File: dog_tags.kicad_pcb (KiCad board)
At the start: 4 copper layers, 0 parts

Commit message: Basic layout for PCB done, including silkscreen
Signed-off-by: Lucy Mielke <user@domain.tld>
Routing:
- added copper zone on F.Cu, net (none)
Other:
- board outline added: 49.4 x 28.1 mm
- board text added: "THIS MACHINE KILLS FASCISTS"
- board text added: "engineering.redlucy404.de"

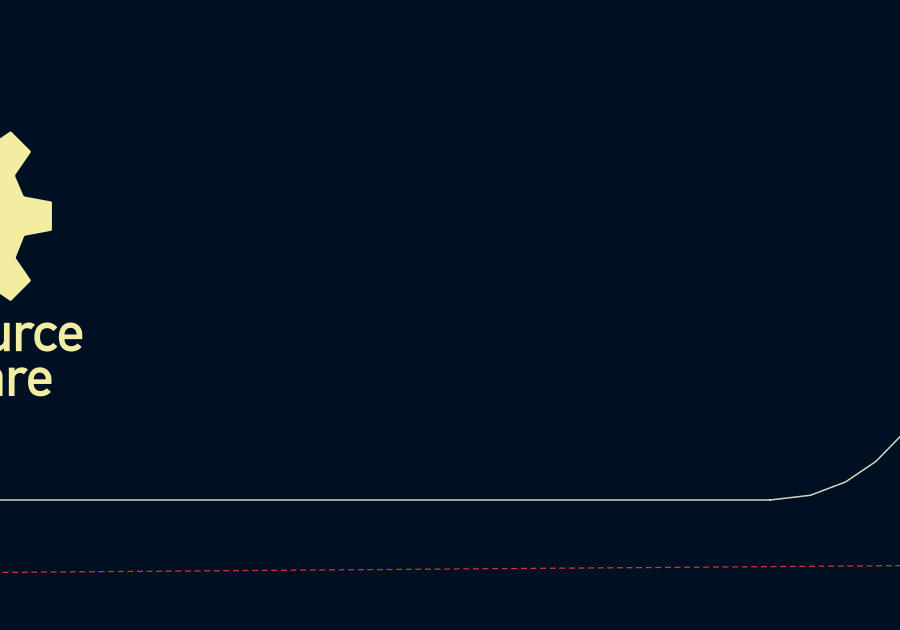
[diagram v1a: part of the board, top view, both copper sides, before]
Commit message: RFID IC placement + keep-out zone
Signed-off-by: Lucy Mielke <user@domain.tld>
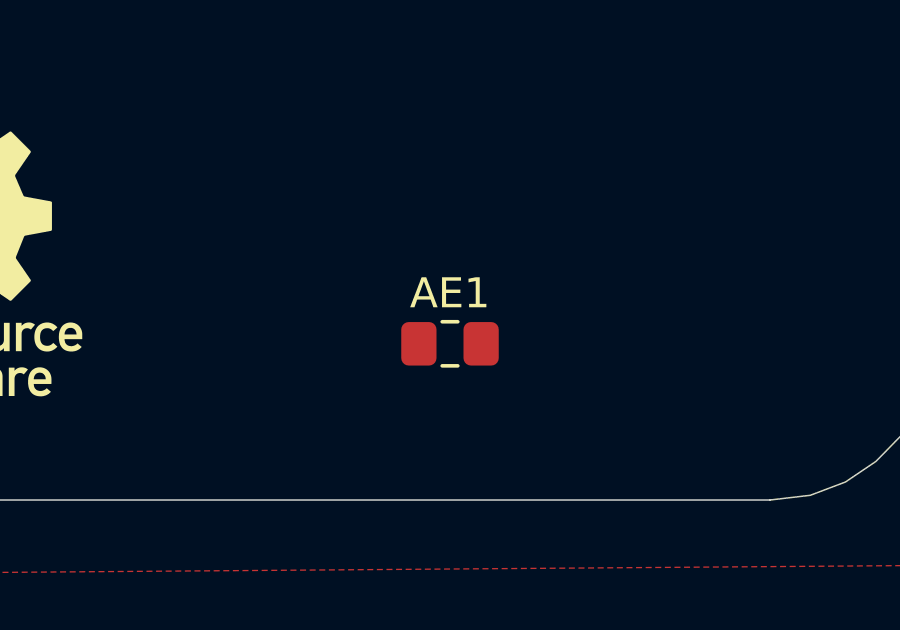
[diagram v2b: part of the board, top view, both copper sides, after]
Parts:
- added AE1: LXMS21ACMD-220, Capacitor_SMD:C_0805_2012Metric_Pad1.18x1.45mm_HandSolder, F.Cu at (145.0, 94.2)
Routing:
- added copper zone on F.Cu, net GND
- removed copper zone on F.Cu, net (none)
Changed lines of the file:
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@@
 		(13 "F.Paste" user)
 		(15 "B.Paste" user)
-		(5 "F.SilkS" user)
-		(7 "B.SilkS" user)
+		(5 "F.SilkS" user "F.Silkscreen")
+		(7 "B.SilkS" user "B.Silkscreen")
 		(1 "F.Mask" user)
 		(3 "B.Mask" user)
 		(25 "Edge.Cuts" user)
 		(27 "Margin" user)
-		(31 "F.CrtYd" user)
-		(29 "B.CrtYd" user)
+		(31 "F.CrtYd" user "F.Courtyard")
+		(29 "B.CrtYd" user "B.Courtyard")
 		(35 "F.Fab" user)
 	)
@@
 		(capping no)
 		(filling no)
-		(zone_defaults)
 		(pcbplotparams
 			(layerselection 0x00000000_00000000_55555555_5755f5ff)
@@
 	(property "REVISION" "1.0")
 	(property "TITLE" "Dog Tags")
+	(footprint "Capacitor_SMD:C_0805_2012Metric_Pad1.18x1.45mm_HandSolder"
+		(layer "F.Cu")
+		(at 145.034 94.234)
+		(descr "Capacitor SMD 0805 (2012 Metric), square (rectangular) end terminal, IPC-7351 nominal with elongated pad for handsoldering. (Body size source: IPC-SM-782 page 76, https://www.pcb-3d.com/wordpress/wp-content/uploads/ipc-sm-782a_amendment_1_and_2.pdf, https://docs.google.com/spreadsheets/d/1BsfQQcO9C6DZCsRaXUlFlo91Tg2WpOkGARC1WS5S8t0/edit?usp=sharing)")
+		(tags "capacitor handsolder")
+		(property "Reference" "AE1"
+			(at 0 -1.68 0)
+			(layer "F.SilkS")
+			(effects
+				(font
+					(size 1 1)
+					(thickness 0.15)
+				)
+			)
+		)
+		(property "Value" "LXMS21ACMD-220"
+			(at 0 1.68 0)
+			(layer "F.Fab")
+			(effects
+				(font
+					(size 1 1)
+					(thickness 0.15)
+				)
+			)
+		)
+		(property "Datasheet" ""
+			(at 0 0 0)
+			(layer "F.Fab")
+			(hide yes)
+			(effects
+				(font
+					(size 1.27 1.27)
+				)
+			)
+		)
+		(property "Description" "Dipole antenna"
+			(at 0 0 0)
+			(layer "F.Fab")
+			(hide yes)
+			(effects
+				(font
+					(size 1.27 1.27)
+				)
+			)
+		)
+		(property "KiLib_Generator" "SMD_2terminal_chip_molded"
+			(at 0 0 0)
+			(layer "F.SilkS")
+			(hide yes)
+			(effects
+				(font
+					(size 1 1)
+					(thickness 0.15)
+				)
+			)
+		)
+		(sheetname "/")
+		(sheetfile "dog_tags.kicad_sch")
+		(units
+			(unit
+				(name "A")
+				(pins "1" "2")
+			)
+		)
+		(attr smd)
+		(duplicate_pad_numbers_are_jumpers no)
+		(fp_line
+			(start -0.261252 -0.735)
+			(end 0.261252 -0.735)
+			(stroke
+				(width 0.12)
+				(type solid)
+			)
+			(layer "F.SilkS")
+		)
+		(fp_line
+			(start -0.261252 0.735)
+			(end 0.261252 0.735)
+			(stroke
+				(width 0.12)
+				(type solid)
+			)
+			(layer "F.SilkS")
+		)
+		(fp_rect
+			(start -1.88 -0.98)
+			(end 1.88 0.98)
+			(stroke
+				(width 0.05)
+				(type solid)
+			)
+			(fill no)
+			(layer "F.CrtYd")
+		)
+		(fp_rect
+			(start -1 -0.625)
+			(end 1 0.625)
+			(stroke
+				(width 0.1)
+				(type solid)
+			)
+			(fill no)
+			(layer "F.Fab")
+		)
+		(fp_text user "${REFERENCE}"
+			(at 0 0 0)
+			(layer "F.Fab")
+			(effects
+				(font
+					(size 0.5 0.5)
+					(thickness 0.08)
+				)
+			)
+		)
+		(pad "1" smd roundrect
+			(at -1.0375 0)
+			(size 1.175 1.45)
+			(layers "F.Cu" "F.Mask" "F.Paste")
+			(roundrect_rratio 0.212766)
+			(net "GND")
+			(pintype "input")
+		)
+		(pad "2" smd roundrect
+			(at 1.0375 0)
+			(size 1.175 1.45)
+			(layers "F.Cu" "F.Mask" "F.Paste")
+			(roundrect_rratio 0.212766)
+			(net "GND")
+			(pintype "input")
+		)
+		(embedded_fonts no)
+		(model "${KICAD10_3DMODEL_DIR}/Capacitor_SMD.3dshapes/C_0805_2012Metric.step"
+			(offset
+				(xyz 0 0 0)
+			)
+			(scale
+				(xyz 1 1 1)
+			)
+			(rotate
+				(xyz 0 0 0)
+			)
+		)
+	)
 	(gr_poly
 		(pts
@@
 	)
 	(zone
+		(net "GND")
 		(layer "F.Cu")
 		(name "copper pour")
@@
 			)
 		)
+	)
+	(zone
+		(layers "F.Cu" "B.Cu" "In1.Cu" "In2.Cu")
+		(name "Antenna Keep-Out Zone")
+		(hatch edge 0.5)
+		(connect_pads
+			(clearance 0)
+		)
+		(min_thickness 0.25)
+		(keepout
+			(tracks allowed)
+			(vias allowed)
+			(pads allowed)
+			(copperpour not_allowed)
+			(footprints allowed)
+		)
+		(placement
+			(enabled no)
+			(sheetname "/")
+		)
+		(fill
+			(thermal_gap 0.5)
+			(thermal_bridge_width 0.5)
+			(island_removal_mode 1)
+		)
+		(polygon
+			(pts
+				(xy 139.907 88.941) (xy 149.907 88.941) (xy 149.907 99.441) (xy 139.907 99.441)
+			)
+		)

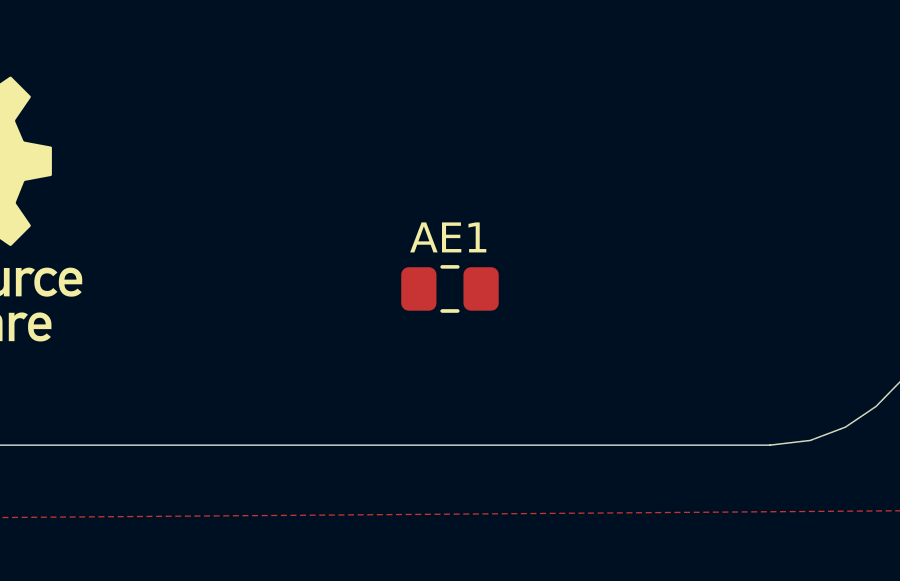
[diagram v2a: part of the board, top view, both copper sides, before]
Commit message: Route antenna trace
Signed-off-by: Lucy Mielke <user@domain.tld>
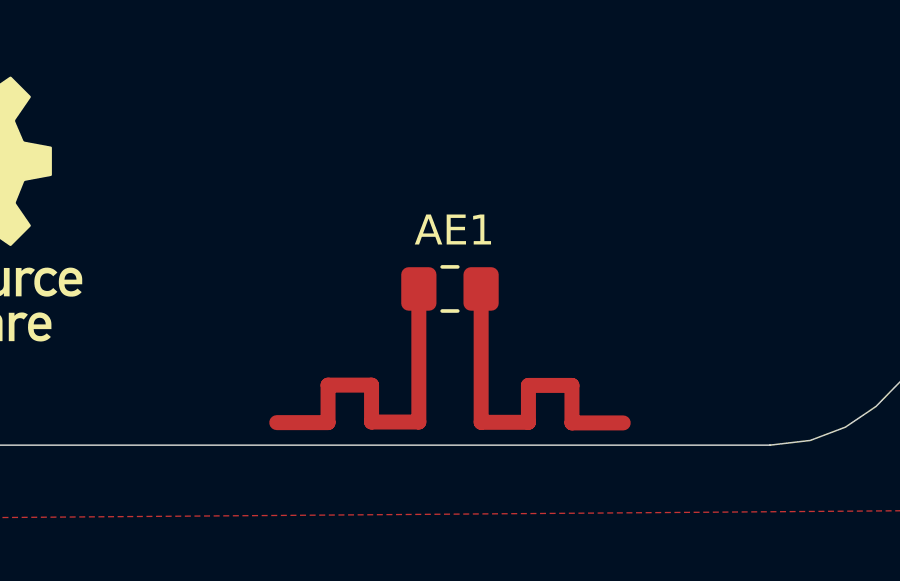
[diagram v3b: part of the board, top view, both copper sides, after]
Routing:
- net GND: track 0.00 -> 23.3 mm

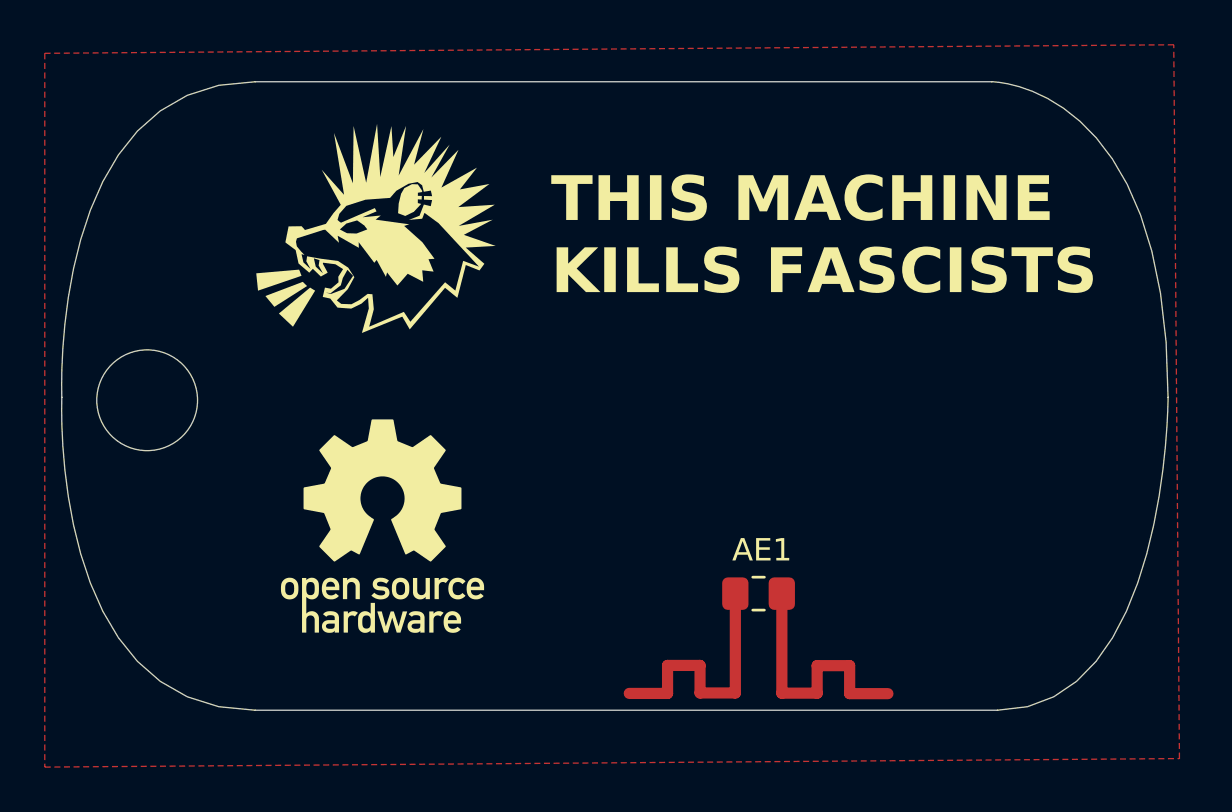
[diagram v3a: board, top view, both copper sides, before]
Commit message: via stitching technically done
Signed-off-by: Lucy Mielke <user@domain.tld>
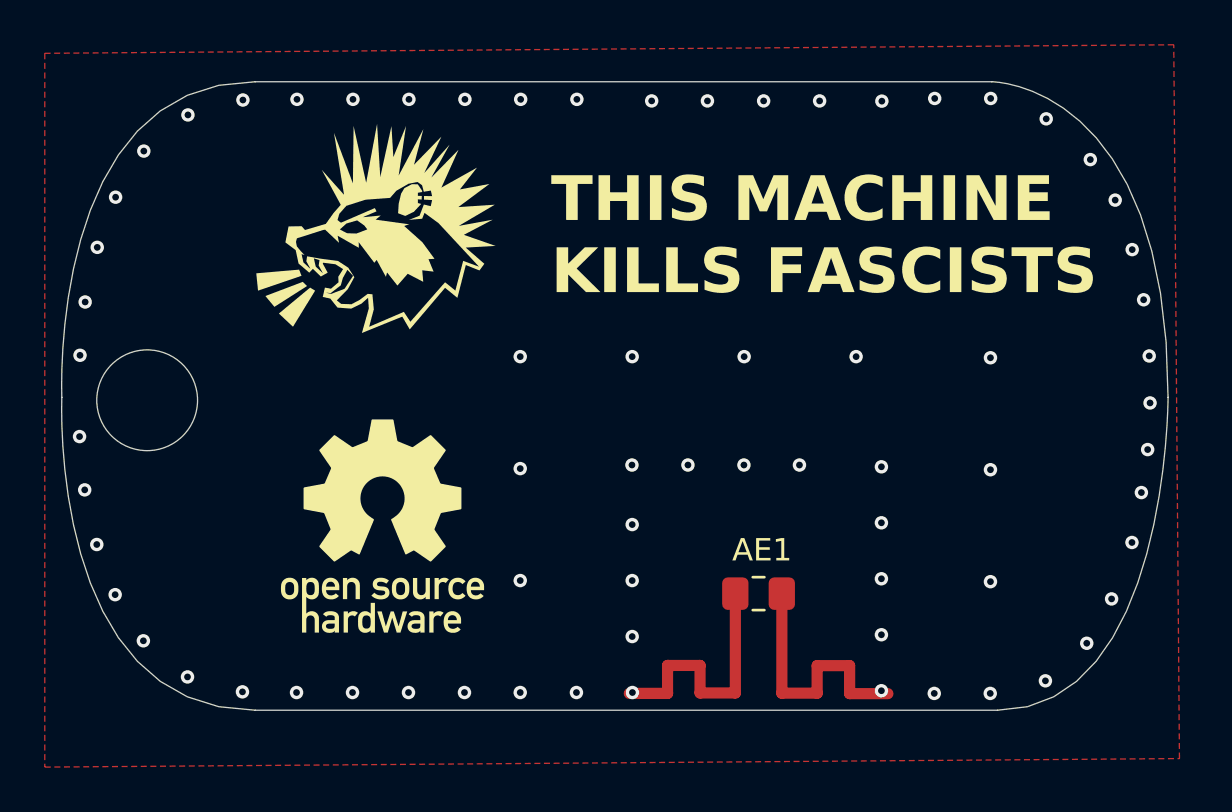
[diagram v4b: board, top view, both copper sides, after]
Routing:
- net GND: vias 0 -> 70

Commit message: add perfboard holes
Signed-off-by: Lucy Mielke <user@domain.tld>
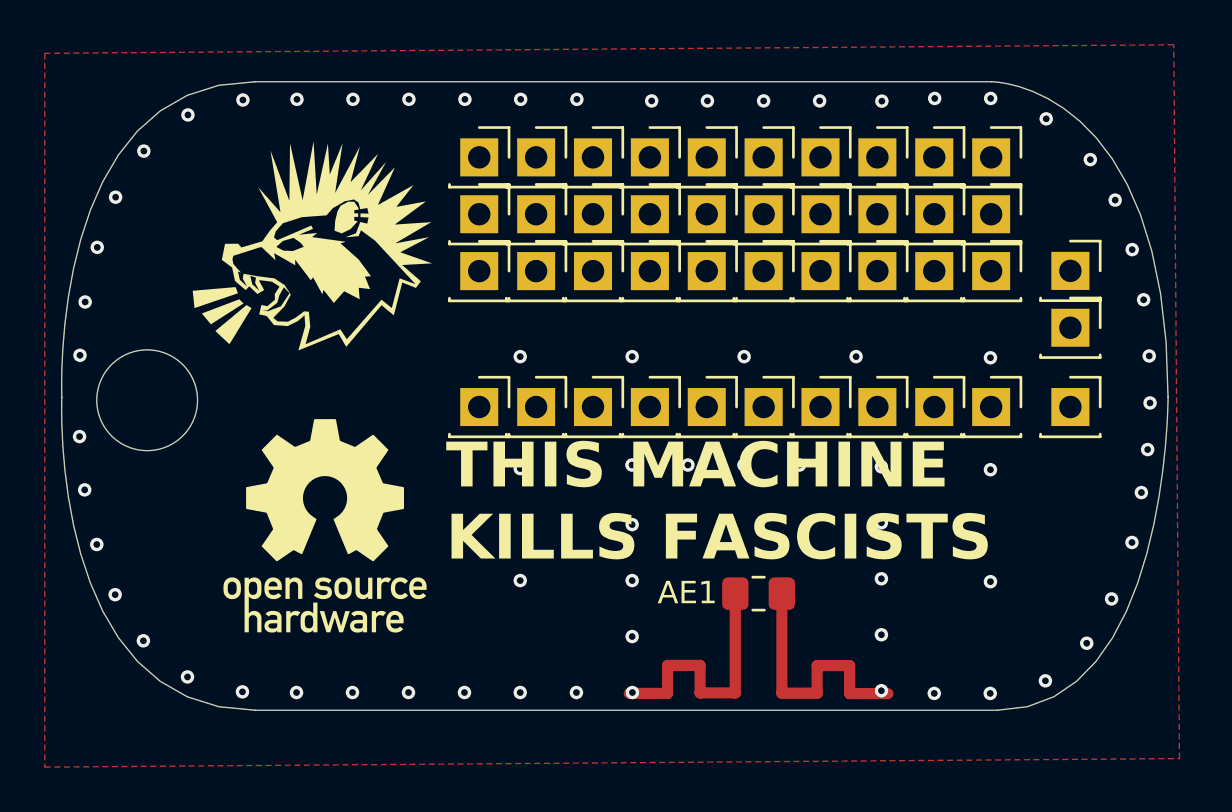
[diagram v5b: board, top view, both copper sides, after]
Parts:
- added TP1: TestPoint, Connector_PinSocket_2.54mm:PinSocket_1x01_P2.54mm_Vertical, F.Cu at (132.6, 74.8)
- added TP10: TestPoint, Connector_PinSocket_2.54mm:PinSocket_1x01_P2.54mm_Vertical, F.Cu at (155.4, 74.8)
- added TP11: TestPoint, Connector_PinSocket_2.54mm:PinSocket_1x01_P2.54mm_Vertical, F.Cu at (132.6, 77.3)
- added TP12: TestPoint, Connector_PinSocket_2.54mm:PinSocket_1x01_P2.54mm_Vertical, F.Cu at (135.1, 77.3)
- added TP13: TestPoint, Connector_PinSocket_2.54mm:PinSocket_1x01_P2.54mm_Vertical, F.Cu at (137.6, 77.3)
- added TP14: TestPoint, Connector_PinSocket_2.54mm:PinSocket_1x01_P2.54mm_Vertical, F.Cu at (140.2, 77.3)
- added TP15: TestPoint, Connector_PinSocket_2.54mm:PinSocket_1x01_P2.54mm_Vertical, F.Cu at (142.7, 77.3)
- added TP16: TestPoint, Connector_PinSocket_2.54mm:PinSocket_1x01_P2.54mm_Vertical, F.Cu at (145.3, 77.3)
- added TP17: TestPoint, Connector_PinSocket_2.54mm:PinSocket_1x01_P2.54mm_Vertical, F.Cu at (147.8, 77.3)
- added TP18: TestPoint, Connector_PinSocket_2.54mm:PinSocket_1x01_P2.54mm_Vertical, F.Cu at (150.3, 77.3)
- added TP19: TestPoint, Connector_PinSocket_2.54mm:PinSocket_1x01_P2.54mm_Vertical, F.Cu at (152.9, 77.3)
- added TP2: TestPoint, Connector_PinSocket_2.54mm:PinSocket_1x01_P2.54mm_Vertical, F.Cu at (135.1, 74.8)
- added TP20: TestPoint, Connector_PinSocket_2.54mm:PinSocket_1x01_P2.54mm_Vertical, F.Cu at (155.4, 77.3)
- added TP21: TestPoint, Connector_PinSocket_2.54mm:PinSocket_1x01_P2.54mm_Vertical, F.Cu at (132.6, 79.8)
- added TP22: TestPoint, Connector_PinSocket_2.54mm:PinSocket_1x01_P2.54mm_Vertical, F.Cu at (135.1, 79.8)
- added TP23: TestPoint, Connector_PinSocket_2.54mm:PinSocket_1x01_P2.54mm_Vertical, F.Cu at (137.6, 79.8)
- added TP24: TestPoint, Connector_PinSocket_2.54mm:PinSocket_1x01_P2.54mm_Vertical, F.Cu at (140.2, 79.8)
- added TP25: TestPoint, Connector_PinSocket_2.54mm:PinSocket_1x01_P2.54mm_Vertical, F.Cu at (142.7, 79.8)
- added TP26: TestPoint, Connector_PinSocket_2.54mm:PinSocket_1x01_P2.54mm_Vertical, F.Cu at (145.3, 79.8)
- added TP27: TestPoint, Connector_PinSocket_2.54mm:PinSocket_1x01_P2.54mm_Vertical, F.Cu at (147.8, 79.8)
- added TP28: TestPoint, Connector_PinSocket_2.54mm:PinSocket_1x01_P2.54mm_Vertical, F.Cu at (150.3, 79.8)
- added TP29: TestPoint, Connector_PinSocket_2.54mm:PinSocket_1x01_P2.54mm_Vertical, F.Cu at (152.9, 79.8)
- added TP3: TestPoint, Connector_PinSocket_2.54mm:PinSocket_1x01_P2.54mm_Vertical, F.Cu at (137.6, 74.8)
- added TP30: TestPoint, Connector_PinSocket_2.54mm:PinSocket_1x01_P2.54mm_Vertical, F.Cu at (155.4, 79.8)
- added TP4: TestPoint, Connector_PinSocket_2.54mm:PinSocket_1x01_P2.54mm_Vertical, F.Cu at (140.2, 74.8)
- added TP41: TestPoint, Connector_PinSocket_2.54mm:PinSocket_1x01_P2.54mm_Vertical, F.Cu at (132.6, 85.9)
- added TP42: TestPoint, Connector_PinSocket_2.54mm:PinSocket_1x01_P2.54mm_Vertical, F.Cu at (135.1, 85.9)
- added TP43: TestPoint, Connector_PinSocket_2.54mm:PinSocket_1x01_P2.54mm_Vertical, F.Cu at (137.6, 85.9)
- added TP44: TestPoint, Connector_PinSocket_2.54mm:PinSocket_1x01_P2.54mm_Vertical, F.Cu at (140.2, 85.9)
- added TP45: TestPoint, Connector_PinSocket_2.54mm:PinSocket_1x01_P2.54mm_Vertical, F.Cu at (142.7, 85.9)
- added TP46: TestPoint, Connector_PinSocket_2.54mm:PinSocket_1x01_P2.54mm_Vertical, F.Cu at (145.3, 85.9)
- added TP47: TestPoint, Connector_PinSocket_2.54mm:PinSocket_1x01_P2.54mm_Vertical, F.Cu at (147.8, 85.9)
- added TP48: TestPoint, Connector_PinSocket_2.54mm:PinSocket_1x01_P2.54mm_Vertical, F.Cu at (150.3, 85.9)
- added TP49: TestPoint, Connector_PinSocket_2.54mm:PinSocket_1x01_P2.54mm_Vertical, F.Cu at (159.0, 85.9)
- added TP5: TestPoint, Connector_PinSocket_2.54mm:PinSocket_1x01_P2.54mm_Vertical, F.Cu at (142.7, 74.8)
- added TP50: TestPoint, Connector_PinSocket_2.54mm:PinSocket_1x01_P2.54mm_Vertical, F.Cu at (159.0, 79.8)
- added TP51: TestPoint, Connector_PinSocket_2.54mm:PinSocket_1x01_P2.54mm_Vertical, F.Cu at (152.9, 85.9)
- added TP52: TestPoint, Connector_PinSocket_2.54mm:PinSocket_1x01_P2.54mm_Vertical, F.Cu at (155.4, 85.9)
- added TP6: TestPoint, Connector_PinSocket_2.54mm:PinSocket_1x01_P2.54mm_Vertical, F.Cu at (145.3, 74.8)
- added TP60: TestPoint, Connector_PinSocket_2.54mm:PinSocket_1x01_P2.54mm_Vertical, F.Cu at (159.0, 82.4)
- added TP7: TestPoint, Connector_PinSocket_2.54mm:PinSocket_1x01_P2.54mm_Vertical, F.Cu at (147.8, 74.8)
- added TP8: TestPoint, Connector_PinSocket_2.54mm:PinSocket_1x01_P2.54mm_Vertical, F.Cu at (150.3, 74.8)
- added TP9: TestPoint, Connector_PinSocket_2.54mm:PinSocket_1x01_P2.54mm_Vertical, F.Cu at (152.9, 74.8)
